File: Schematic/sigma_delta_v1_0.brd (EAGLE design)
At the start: 160 x 100 mm, 65 parts, among them IC1 LM50, IC2 MC78M12CDTG, IC3 UA78M33DCY, IC4 LM50, IC5 ACPL-064L-000E, J1 SJ1-3523N, Q3 IRF3707S, Q4 IRF3707S, Q5 BSD223P, X1 1751251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

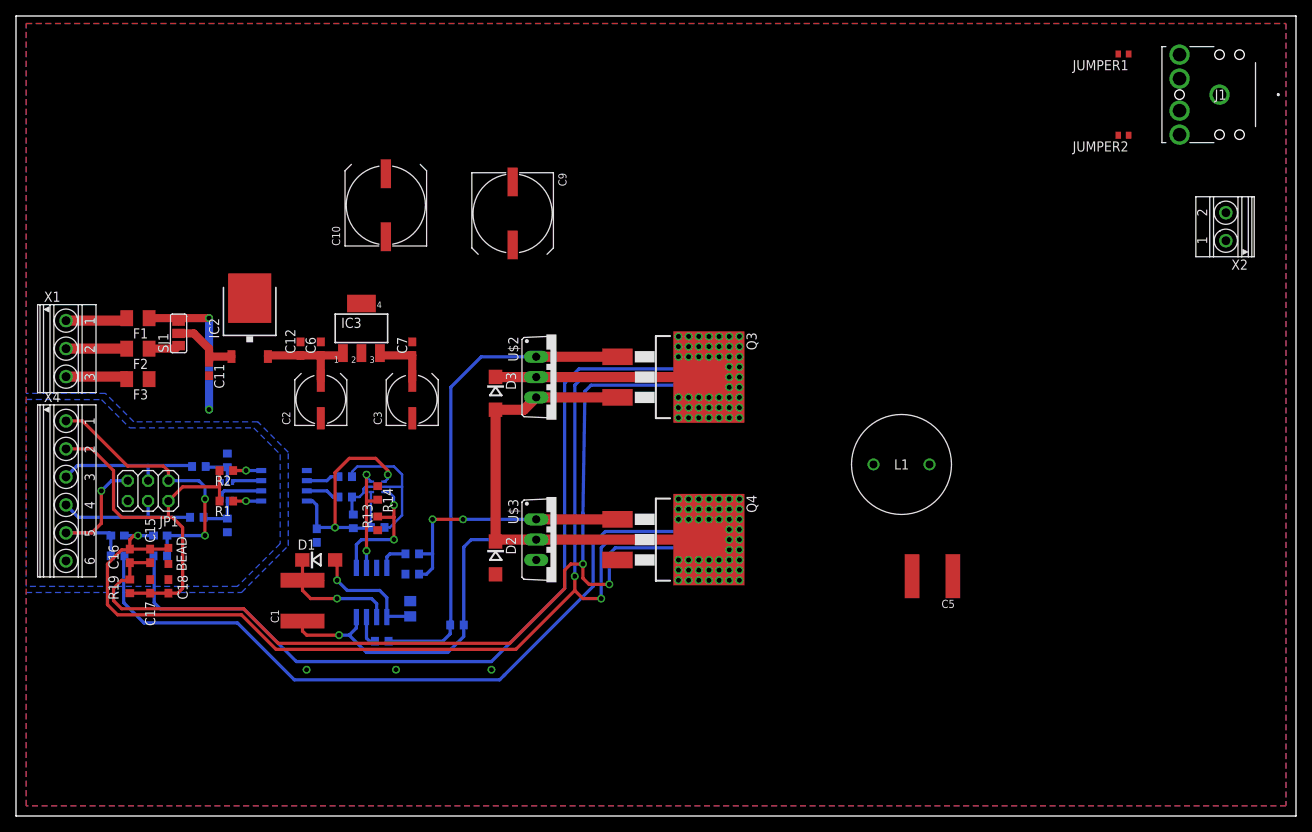
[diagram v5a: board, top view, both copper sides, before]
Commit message: added FPGA_GND polygon to the top layer
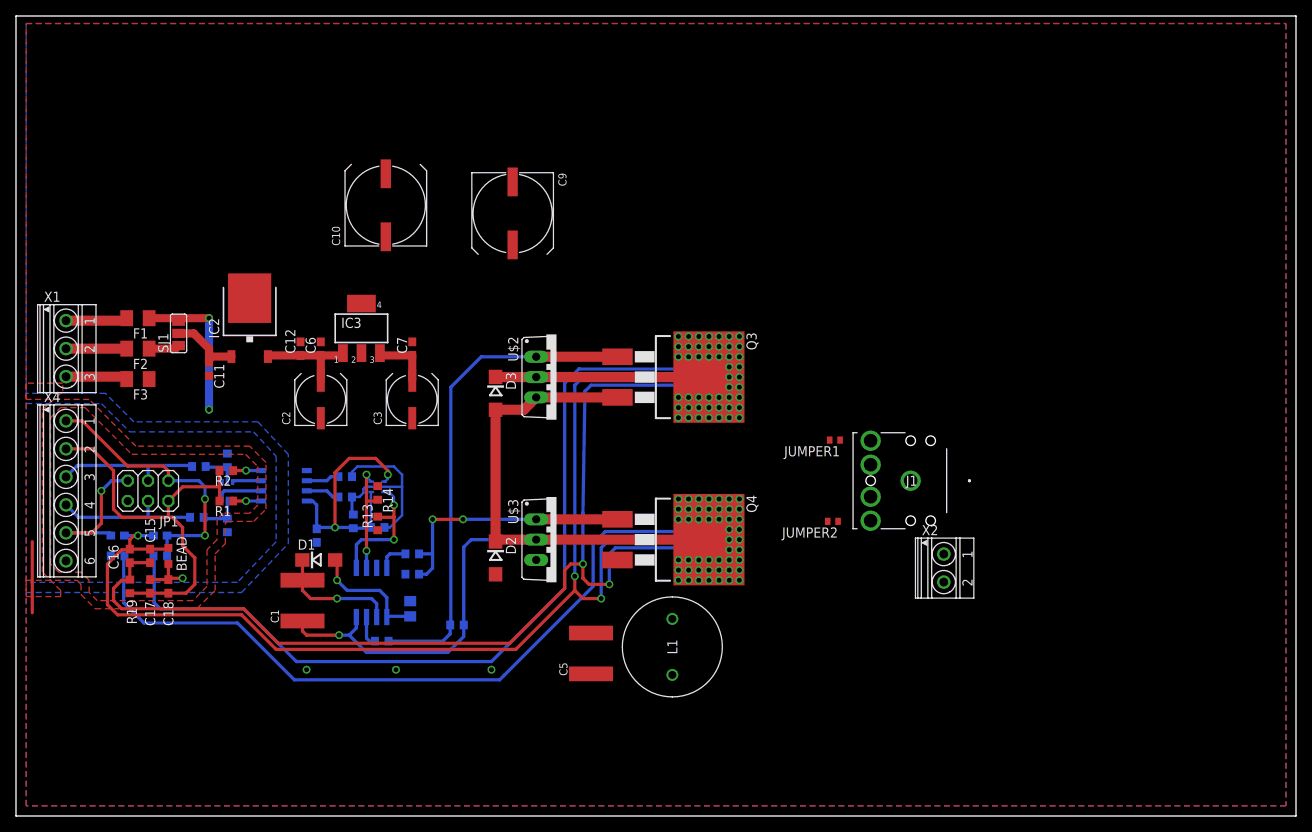
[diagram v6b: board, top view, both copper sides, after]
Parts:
- moved J1 61.8 mm to (116.3, 41.9)
- moved JUMPER2 60.4 mm to (102.1, 36.8)
- moved JUMPER1 60.2 mm to (102.4, 47.0)
- moved X2 55.2 mm to (116.1, 31.0), turned to 270 degrees
- moved C5 43.7 mm to (71.9, 20.3), turned to 90 degrees
- moved L1 31.7 mm to (82.0, 24.6), turned to 270 degrees
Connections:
- net GND: no longer BEAD.1, C17.2, C18.2
- net GND_FPGA: now also BEAD.1, C17.2, C18.2
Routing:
- net GND: track 0.00 -> 8.89 mm
- net GND_FPGA: track 0.00 -> 6.09 mm, vias 0 -> 1
- net N$29: track 21.2 -> 18.6 mm
- net VCC_FPGA: track 48.9 -> 50.8 mm
- added copper zone on layer 1, net GND_FPGA

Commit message: intermediate commit prior changing the net to mm
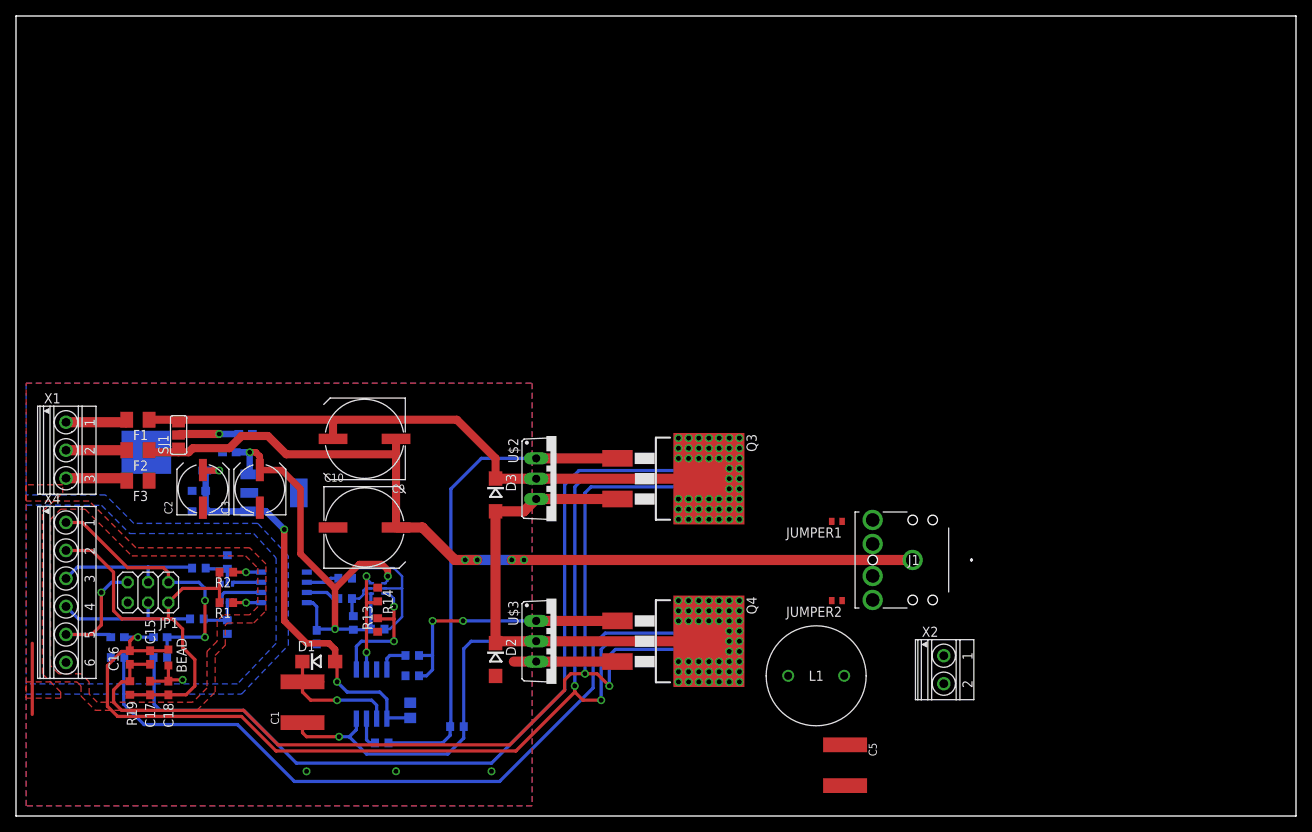
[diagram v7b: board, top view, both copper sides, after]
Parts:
- moved C10 40.4 mm to (43.6, 36.1), turned to 0 degrees
- moved C5 34.7 mm to (103.6, 6.35), turned to 270 degrees
- moved C9 33.7 mm to (43.6, 47.1), turned to 180 degrees
- moved C7 26.3 mm to (26.7, 45.5), flipped to the bottom, turned to 0 degrees
- moved C6 25.4 mm to (22.9, 38.1), flipped to the bottom, turned to 0 degrees
- moved IC3 23.3 mm to (32.3, 40.4), flipped to the bottom, turned to 90 degrees
- moved C3 22.1 mm to (30.5, 40.9)
- moved C12 21.8 mm to (22.9, 40.6), flipped to the bottom, turned to 0 degrees
- moved IC2 19.7 mm to (18.8, 45.5), flipped to the bottom, turned to 270 degrees
- moved C2 18.5 mm to (23.4, 40.9)
- moved L1 16.1 mm to (96.5, 17.5), turned to 0 degrees
- moved C17 12.7 mm to (16.8, 16.0)
- moved C18 12.7 mm to (19.1, 16.0)
- moved D2 12.7 mm to (59.9, 19.6)
- moved D3 12.7 mm to (59.9, 40.1)
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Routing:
- net VCC_MID: track 3.84 -> 114.0 mm, vias 0 -> 4
- net VCC_HI: track 46.0 -> 77.3 mm, vias 50 -> 48
- net VCC_12: track 28.1 -> 55.7 mm, vias 1 -> 3
- net VCC_3.3: track 40.0 -> 60.1 mm, vias 2 -> 3
- net GND: track 8.89 -> 21.8 mm
- net AVCC_FPGA: track 129.7 -> 128.2 mm
- net N$27: track 9.79 -> 9.39 mm, vias 0 -> 1

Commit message: Finished layouting. DRC pending
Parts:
- removed JUMPER1, JUMPER2: 0, resistor:R0402
- added SJ2: (no value), jumper:SJ_2
- moved C5 16.8 mm to (110.7, 21.6), turned to 0 degrees
- moved X2 5.56 mm to (112.5, 14.0)
- moved C10 3.00 mm to (43.6, 39.1)
- moved C12 3.00 mm to (22.9, 43.6)
- moved C17 3.00 mm to (16.8, 19.0)
- moved C18 3.00 mm to (19.1, 19.0)
- moved C2 3.00 mm to (23.4, 43.9)
- moved C3 3.00 mm to (30.5, 43.9)
- moved C7 3.00 mm to (26.7, 48.5)
- moved D1 3.00 mm to (37.8, 22.3)
- moved D3 3.00 mm to (59.9, 43.1)
- moved F1 3.00 mm to (15.2, 52.5)
- moved F2 3.00 mm to (15.2, 48.7)
- moved F3 3.00 mm to (15.2, 44.9)
- moved IC2 3.00 mm to (18.8, 48.5)
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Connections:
- net N$10: now also C5.1, L1.2, SJ2.2, X2.2; no longer J1.3, JUMPER2.1
- net N$24: now also J1.3, SJ2.3; no longer C5.1, JUMPER1.2, JUMPER2.2, L1.2, X2.2
- net N$25: now also SJ2.1; no longer JUMPER1.1
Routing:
- net N$10: track 0.00 -> 41.2 mm, vias 0 -> 2
- net VCC_MID: track 114.0 -> 138.4 mm
- net N$24: track 0.00 -> 8.09 mm
- net N$25: track 0.00 -> 7.75 mm
- net GND: vias 3 -> 57
- added copper zone on layer 1, net H_BRIDGE_MID
- added copper zone on layer 16, net H_BRIDGE_MID
- added copper zone on layer 1, net VCC_HI
- added copper zone on layer 16, net VCC_HI
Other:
- board size 160 x 100 mm -> 120 x 70 mm
